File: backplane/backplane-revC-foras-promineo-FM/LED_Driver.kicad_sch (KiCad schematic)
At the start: 23 parts, among them Q602 BC857AW,115, Q603 BC847CW,115

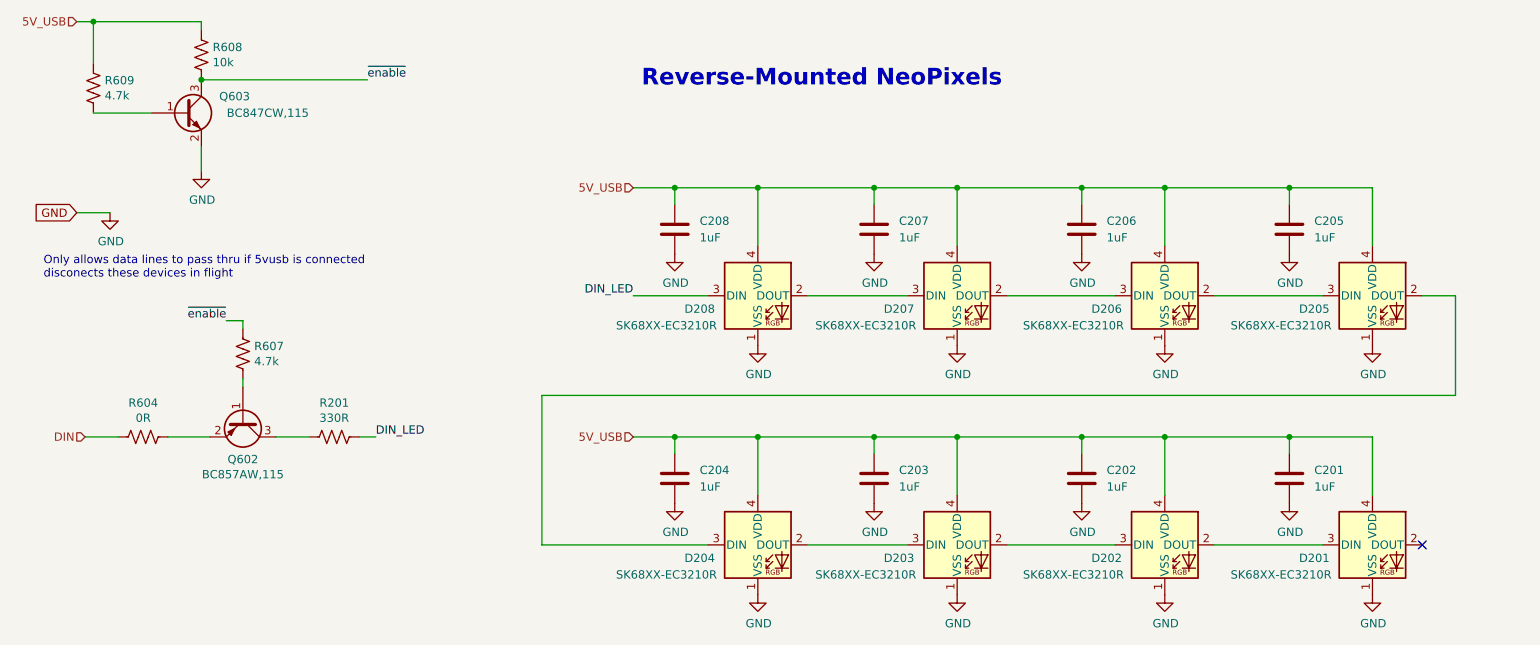
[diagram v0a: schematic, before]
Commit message: added rbf_ret net, added capability for neopixels on BP cards, added jumpers to bypass this
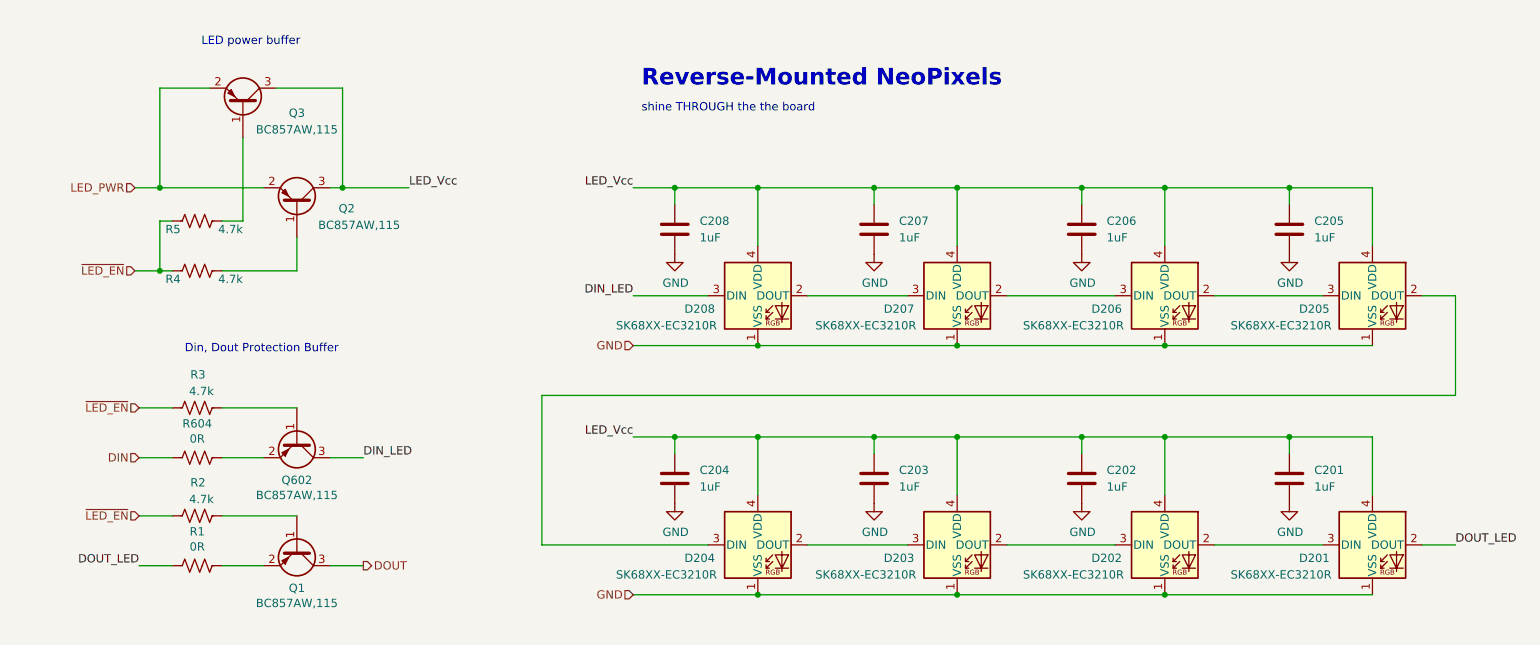
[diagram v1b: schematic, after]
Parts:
- removed Q603: BC847CW,115, Package_TO_SOT_SMD:SOT-323_SC-70, symbol backplane-rescue:Q_NPN_BEC-Device
- removed R201: 330R, Resistor_SMD:R_0402_1005Metric, symbol backplane-rescue:R_US-Device
- removed R607, R609: 4.7k, Resistor_SMD:R_0402_1005Metric, symbol backplane-rescue:R_US-Device
- removed R608: 10k, Resistor_SMD:R_0402_1005Metric, symbol backplane-rescue:R_US-Device
- added Q1, Q2, Q3: BC857AW,115, Package_TO_SOT_SMD:SOT-323_SC-70, symbol backplane-rescue:Q_PNP_BEC-Device
- added R1: 0R, Resistor_SMD:R_0402_1005Metric, symbol backplane-rescue:R_US-Device
- added R2, R3, R4, R5: 4.7k, Resistor_SMD:R_0402_1005Metric, symbol backplane-rescue:R_US-Device
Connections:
- net DIN_LED: now also Q602.3 (C)
- net at Q602.1 (B): now also R3.2
- net DOUT_LED: now reaches D201.2 (DOUT)
- net DOUT_LED: now also R1.2
- net 5V_USB renamed LED_Vcc
- net LED_Vcc: now also Q2.3 (C), Q3.3 (C)
- new net: Q2.1 (B), R4.2
- new net: Q1.2 (E), R1.1
- new net: Q1.1 (B), R2.2
- new net: Q3.1 (B), R5.2
- new net DOUT: Q1.3 (C)
- new net LED_PWR: Q2.2 (E), Q3.2 (E)
- new net ~{LED_EN}: R2.1, R3.1, R4.1, R5.1
- no-connect marks 1 -> 0
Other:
- note added: "Din, Dout Protection Buffer"
- note added: "LED power buffer"
- note added: "shine THROUGH the the board"
- note removed: "Only allows data lines to pass thru if 5vusb is connected disconects these devices in flight"
- moved on the sheet: Q602, R604
